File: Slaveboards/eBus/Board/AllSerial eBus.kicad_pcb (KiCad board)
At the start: 2 copper layers, 67.4 x 44.8 mm, 40 parts, among them J3 Conn_01x02, Q1 Q_PNP_BCEC, Q2 BC847, Q3 BC857, Q4 BC847, Q5 Q_PNP_BCEC, Q6 BC847, U1 LM293, X1 AllSerial_Connector

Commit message: Improve libraries
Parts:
- D7: footprint LED_SMD:LED_0805_2012Metric -> LED_SMD:LED_0603_1608Metric

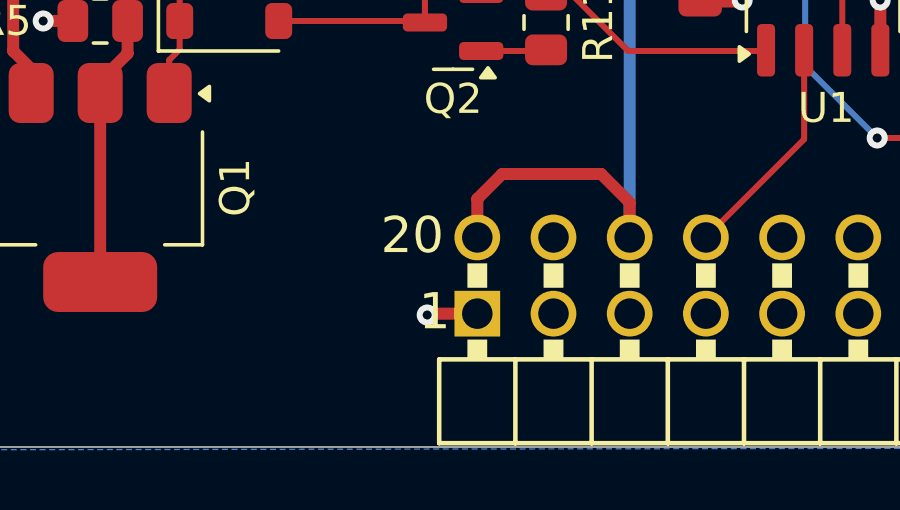
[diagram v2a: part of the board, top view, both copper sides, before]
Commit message: Remove pads from cutouts
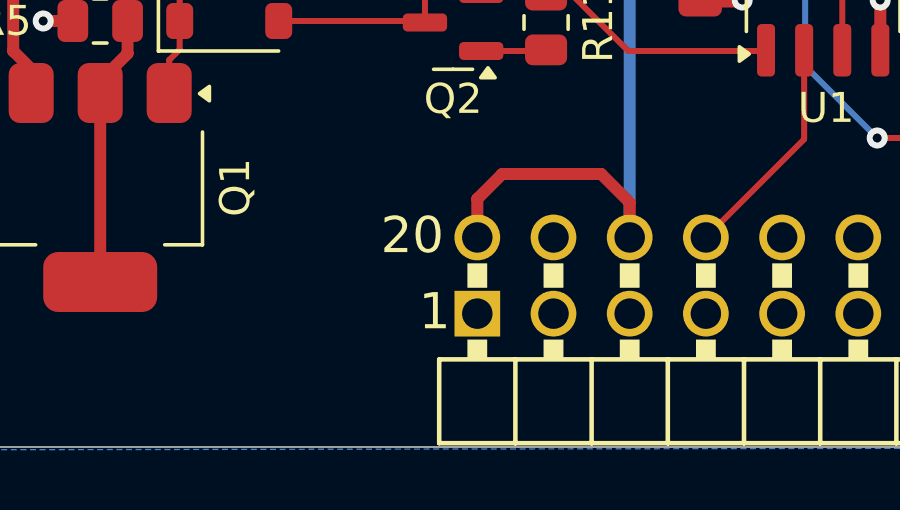
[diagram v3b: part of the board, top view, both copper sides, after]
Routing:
- net GND: track 13.8 -> 12.1 mm, vias 13 -> 12
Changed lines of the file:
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@@
 		)
 		(fp_line
-			(start -35.7 -37)
-			(end 35.8 -37)
-			(stroke
-				(width 0.1)
-				(type default)
-			)
-			(layer "Cmts.User")
-		)
-		(fp_line
 			(start -33.7 -44.8)
 			(end 33.7 -44.8)
@@
 			)
 		)
-		(model "${KICAD_USER_3D_DIR}/Fischer AKG 71 24 100 bottom half.step"
+		(model "${KICAD9_3RD_PARTY}/packages3d/Fischer AKG 71 24 100 bottom half.step"
 			(offset
 				(xyz 35.8 44.8 1.85)
@@
 			)
 		)
+		(model "../Front/AllSerial eBUS Front.step"
+			(offset
+				(xyz 0 44.8 -7.25)
+			)
+			(scale
+				(xyz 1 1 1)
+			)
+			(rotate
+				(xyz -90 -0 180)
+			)
+		)
 	)
 	(footprint "Resistor_SMD:R_0805_2012Metric"
@@
 	)
 	(segment
-		(start 138.14 114)
-		(end 136.515 114)
-		(width 0.4)
-		(layer "F.Cu")
-		(net 19)
-	)
-	(segment
-		(start 136.515 114)
-		(end 136.47 114.045)
-		(width 0.4)
-		(layer "F.Cu")
-		(net 19)
-	)
-	(segment
 		(start 127.37 93.895)
 		(end 127.37 94.645)
@@
 		(net 19)
 	)
-	(via
-		(at 136.47 114.045)
-		(size 0.7)
-		(drill 0.3)
-		(layers "F.Cu" "B.Cu")
-		(net 19)
-	)
